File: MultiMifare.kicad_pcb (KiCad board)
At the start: 2 copper layers, 54 x 85.6 mm, 5 parts, among them SW1 SW_SPST, SW2 SW_SPST, U1 Mifare_Chip, U2 Mifare_Chip

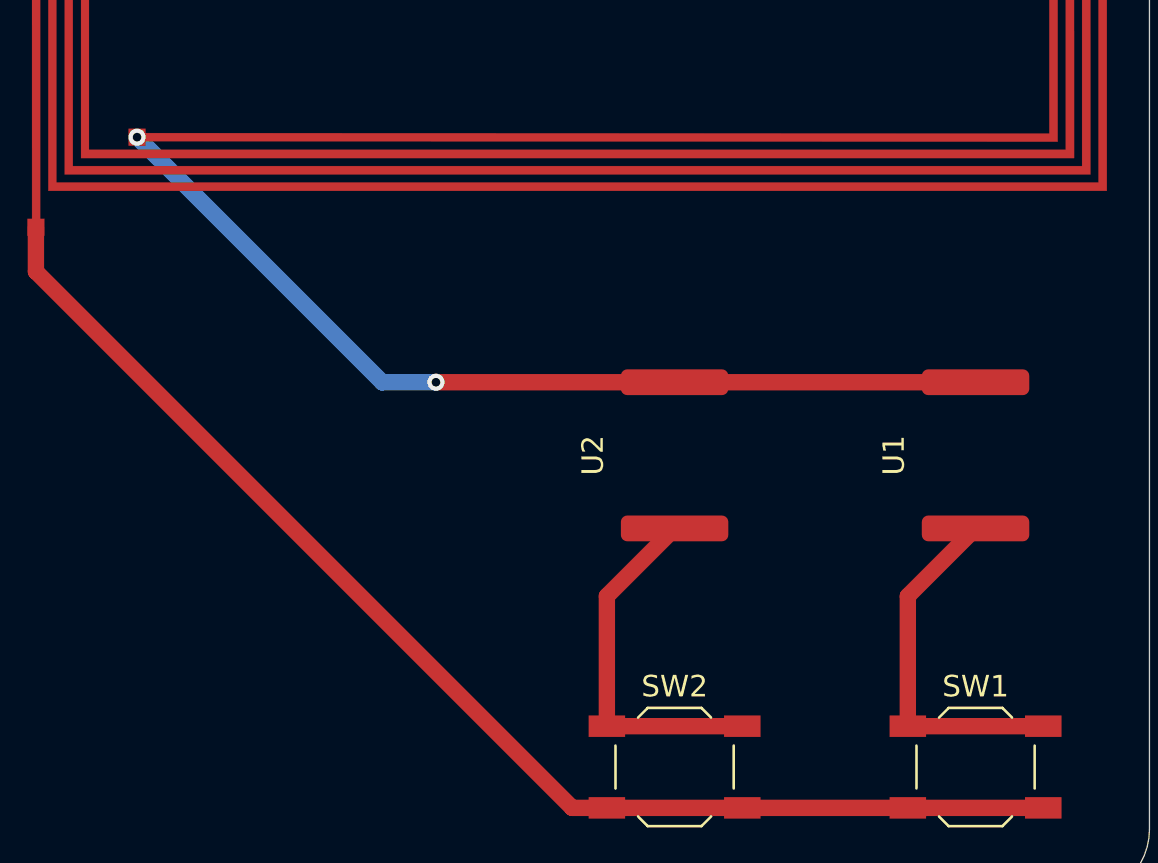
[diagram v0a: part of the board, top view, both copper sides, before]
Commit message: Easier to solder
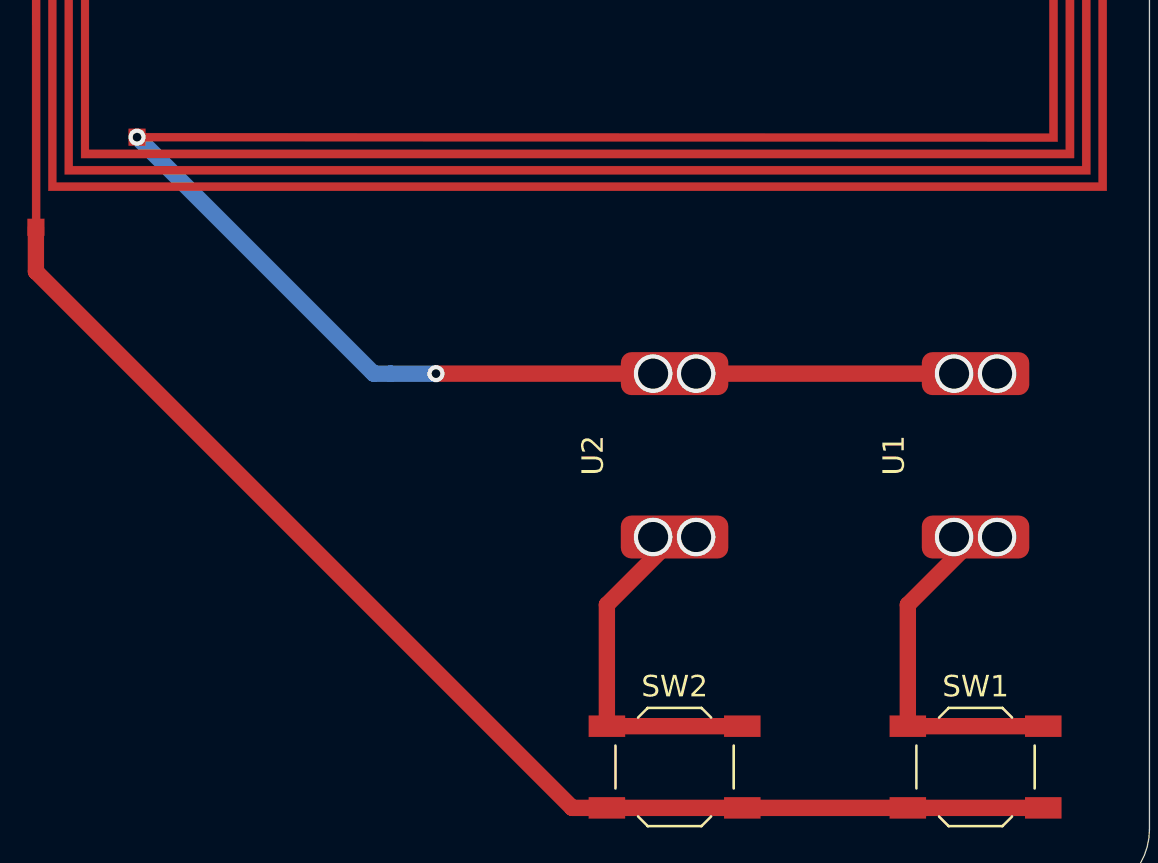
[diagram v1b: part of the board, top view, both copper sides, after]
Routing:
- net Net-(SW2-Pad1): track 16.8 -> 16.4 mm, vias 0 -> 2
- net Net-(SW1-Pad1): track 16.8 -> 16.4 mm, vias 0 -> 2
- net Net-(AE1-Pad2): track 43.7 -> 43.6 mm, vias 2 -> 6
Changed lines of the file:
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@@
     (thickness 1.6)
     (drawings 8)
-    (tracks 21)
+    (tracks 29)
     (zones 0)
     (modules 5)
@@
     (34 B.Paste user)
     (35 F.Paste user)
-    (36 B.SilkS user hide)
-    (37 F.SilkS user hide)
+    (36 B.SilkS user)
+    (37 F.SilkS user)
     (38 B.Mask user)
-    (39 F.Mask user hide)
+    (39 F.Mask user)
     (40 Dwgs.User user)
     (41 Cmts.User user)
@@
   )
   (setup
-    (last_trace_width 0.25)
+    (last_trace_width 0.762)
     (user_trace_width 0.254)
     (user_trace_width 0.508)
@@
       (effects (font (size 1 1) (thickness 0.15)))
     )
+    (fp_line (start -5.08 -2.8) (end 5.08 -2.8) (layer F.CrtYd) (width 0.12))
+    (fp_line (start 5.08 -2.8) (end 5.08 2.8) (layer F.CrtYd) (width 0.12))
+    (fp_line (start 5.08 2.8) (end -5.08 2.8) (layer F.CrtYd) (width 0.12))
+    (fp_line (start -5.08 2.8) (end -5.08 -2.8) (layer F.CrtYd) (width 0.12))
+    (fp_line (start -2.5 -2.4) (end 2.5 -2.4) (layer F.Fab) (width 0.12))
+    (fp_line (start 2.5 -2.4) (end 2.5 2.4) (layer F.Fab) (width 0.12))
+    (fp_line (start 2.5 2.4) (end -2.5 2.4) (layer F.Fab) (width 0.12))
     (fp_line (start -2.5 2.4) (end -2.5 -2.4) (layer F.Fab) (width 0.12))
-    (fp_line (start 2.5 2.4) (end -2.5 2.4) (layer F.Fab) (width 0.12))
-    (fp_line (start 2.5 -2.4) (end 2.5 2.4) (layer F.Fab) (width 0.12))
-    (fp_line (start -2.5 -2.4) (end 2.5 -2.4) (layer F.Fab) (width 0.12))
-    (fp_line (start -4.3 2.8) (end -4.3 -2.8) (layer F.CrtYd) (width 0.12))
-    (fp_line (start 4.3 2.8) (end -4.3 2.8) (layer F.CrtYd) (width 0.12))
-    (fp_line (start 4.3 -2.8) (end 4.3 2.8) (layer F.CrtYd) (width 0.12))
-    (fp_line (start -4.3 -2.8) (end 4.3 -2.8) (layer F.CrtYd) (width 0.12))
-    (pad 2 smd roundrect (at 3.4 0 270) (size 1.2 5) (layers F.Cu F.Paste F.Mask) (roundrect_rratio 0.25)
+    (pad 2 smd roundrect (at 3.8 0 270) (size 2 5) (layers F.Cu F.Paste F.Mask) (roundrect_rratio 0.25)
       (net 2 "Net-(SW2-Pad1)"))
-    (pad 1 smd roundrect (at -3.4 0 270) (size 1.2 5) (layers F.Cu F.Paste F.Mask) (roundrect_rratio 0.25)
+    (pad 1 smd roundrect (at -3.8 0 270) (size 2 5) (layers F.Cu F.Paste F.Mask) (roundrect_rratio 0.25)
       (net 4 "Net-(AE1-Pad2)"))
   )
@@
       (effects (font (size 1 1) (thickness 0.15)))
     )
+    (fp_line (start -5.08 -2.8) (end 5.08 -2.8) (layer F.CrtYd) (width 0.12))
+    (fp_line (start 5.08 -2.8) (end 5.08 2.8) (layer F.CrtYd) (width 0.12))
+    (fp_line (start 5.08 2.8) (end -5.08 2.8) (layer F.CrtYd) (width 0.12))
+    (fp_line (start -5.08 2.8) (end -5.08 -2.8) (layer F.CrtYd) (width 0.12))
+    (fp_line (start -2.5 -2.4) (end 2.5 -2.4) (layer F.Fab) (width 0.12))
+    (fp_line (start 2.5 -2.4) (end 2.5 2.4) (layer F.Fab) (width 0.12))
+    (fp_line (start 2.5 2.4) (end -2.5 2.4) (layer F.Fab) (width 0.12))
     (fp_line (start -2.5 2.4) (end -2.5 -2.4) (layer F.Fab) (width 0.12))
-    (fp_line (start 2.5 2.4) (end -2.5 2.4) (layer F.Fab) (width 0.12))
-    (fp_line (start 2.5 -2.4) (end 2.5 2.4) (layer F.Fab) (width 0.12))
-    (fp_line (start -2.5 -2.4) (end 2.5 -2.4) (layer F.Fab) (width 0.12))
-    (fp_line (start -4.3 2.8) (end -4.3 -2.8) (layer F.CrtYd) (width 0.12))
-    (fp_line (start 4.3 2.8) (end -4.3 2.8) (layer F.CrtYd) (width 0.12))
-    (fp_line (start 4.3 -2.8) (end 4.3 2.8) (layer F.CrtYd) (width 0.12))
-    (fp_line (start -4.3 -2.8) (end 4.3 -2.8) (layer F.CrtYd) (width 0.12))
-    (pad 2 smd roundrect (at 3.4 0 270) (size 1.2 5) (layers F.Cu F.Paste F.Mask) (roundrect_rratio 0.25)
+    (pad 2 smd roundrect (at 3.8 0 270) (size 2 5) (layers F.Cu F.Paste F.Mask) (roundrect_rratio 0.25)
       (net 1 "Net-(SW1-Pad1)"))
-    (pad 1 smd roundrect (at -3.4 0 270) (size 1.2 5) (layers F.Cu F.Paste F.Mask) (roundrect_rratio 0.25)
+    (pad 1 smd roundrect (at -3.8 0 270) (size 2 5) (layers F.Cu F.Paste F.Mask) (roundrect_rratio 0.25)
       (net 4 "Net-(AE1-Pad2)"))
   )
@@
     )
     (fp_text value SW_SPST (at 0 3.75) (layer F.Fab)
+      (effects (font (size 1 1) (thickness 0.15)))
+    )
+    (fp_text user %R (at 0 -3.75) (layer F.Fab)
       (effects (font (size 1 1) (thickness 0.15)))
     )
@@
     (fp_line (start -4.25 3) (end -4.25 -3) (layer F.CrtYd) (width 0.05))
     (fp_circle (center 0 0) (end 1 0) (layer F.Fab) (width 0.1))
-    (fp_text user %R (at 0 -3.75) (layer F.Fab)
-      (effects (font (size 1 1) (thickness 0.15)))
-    )
     (pad 2 smd rect (at 3.15 1.9) (size 1.7 1) (layers F.Cu F.Paste F.Mask)
       (net 3 "Net-(AE1-Pad1)"))
@@
     )
     (fp_text value SW_SPST (at 0 3.75) (layer F.Fab)
+      (effects (font (size 1 1) (thickness 0.15)))
+    )
+    (fp_text user %R (at 0 -3.75) (layer F.Fab)
       (effects (font (size 1 1) (thickness 0.15)))
     )
@@
     (fp_line (start -4.25 3) (end -4.25 -3) (layer F.CrtYd) (width 0.05))
     (fp_circle (center 0 0) (end 1 0) (layer F.Fab) (width 0.1))
-    (fp_text user %R (at 0 -3.75) (layer F.Fab)
-      (effects (font (size 1 1) (thickness 0.15)))
-    )
     (pad 2 smd rect (at 3.15 1.9) (size 1.7 1) (layers F.Cu F.Paste F.Mask)
       (net 3 "Net-(AE1-Pad1)"))
@@
   (gr_line (start 179.09 58.16) (end 179.09 137.4) (layer Edge.Cuts) (width 0.05))
   (gr_line (start 128.29 54.98) (end 175.91 54.98) (layer Edge.Cuts) (width 0.05))
-  (segment (start 167.85 126.55) (end 171 123.4) (width 0.762) (layer F.Cu) (net 1))
-  (segment (start 167.85 132.6) (end 167.85 126.55) (width 0.762) (layer F.Cu) (net 1))
+  (via (at 172 123.8) (size 1.8) (drill 1.4) (layers F.Cu B.Cu) (net 1))
+  (via (at 170 123.8) (size 1.8) (drill 1.4) (layers F.Cu B.Cu) (net 1))
+  (via (at 156 123.8) (size 1.8) (drill 1.4) (layers F.Cu B.Cu) (net 2))
+  (via (at 158 123.8) (size 1.8) (drill 1.4) (layers F.Cu B.Cu) (net 2))
+  (via (at 172 116.2) (size 1.8) (drill 1.4) (layers F.Cu B.Cu) (net 4))
+  (via (at 170 116.2) (size 1.8) (drill 1.4) (layers F.Cu B.Cu) (net 4))
+  (via (at 158 116.2) (size 1.8) (drill 1.4) (layers F.Cu B.Cu) (net 4))
   (segment (start 174.15 132.6) (end 167.85 132.6) (width 0.762) (layer F.Cu) (net 1))
+  (segment (start 167.85 126.95) (end 171 123.8) (width 0.762) (layer F.Cu) (net 1))
+  (segment (start 167.85 132.6) (end 167.85 126.95) (width 0.762) (layer F.Cu) (net 1))
   (segment (start 160.15 132.6) (end 153.85 132.6) (width 0.762) (layer F.Cu) (net 2))
-  (segment (start 153.85 126.55) (end 157 123.4) (width 0.762) (layer F.Cu) (net 2))
-  (segment (start 153.85 132.6) (end 153.85 126.55) (width 0.762) (layer F.Cu) (net 2))
+  (segment (start 153.85 126.95) (end 157 123.8) (width 0.762) (layer F.Cu) (net 2))
+  (segment (start 153.85 132.6) (end 153.85 126.95) (width 0.762) (layer F.Cu) (net 2))
   (segment (start 174.15 136.4) (end 167.85 136.4) (width 0.762) (layer F.Cu) (net 3))
   (segment (start 167.85 136.4) (end 160.15 136.4) (width 0.762) (layer F.Cu) (net 3))
@@
   (segment (start 152.238 136.4) (end 127.29 111.452) (width 0.762) (layer F.Cu) (net 3))
   (segment (start 127.29 111.452) (end 127.29 109.392) (width 0.762) (layer F.Cu) (net 3))
-  (segment (start 171 116.6) (end 157 116.6) (width 0.762) (layer F.Cu) (net 4))
-  (via (at 145.9 116.6) (size 0.8) (drill 0.4) (layers F.Cu B.Cu) (net 4))
-  (segment (start 157 116.6) (end 145.9 116.6) (width 0.762) (layer F.Cu) (net 4))
-  (segment (start 143.394 116.6) (end 143.394 116.594) (width 0.762) (layer B.Cu) (net 4))
   (via (at 131.994 105.2) (size 0.8) (drill 0.4) (layers F.Cu B.Cu) (net 4))
+  (via (at 145.9 116.2) (size 0.8) (drill 0.4) (layers F.Cu B.Cu) (net 4))
+  (segment (start 143.788 116.2) (end 145.9 116.2) (width 0.762) (layer B.Cu) (net 4))
   (segment (start 132 105.2) (end 131.994 105.2) (width 0.762) (layer B.Cu) (net 4))
-  (segment (start 143.394 116.594) (end 132 105.2) (width 0.762) (layer B.Cu) (net 4))
-  (segment (start 143.4 116.6) (end 143.394 116.594) (width 0.762) (layer B.Cu) (net 4))
-  (segment (start 145.9 116.6) (end 143.4 116.6) (width 0.762) (layer B.Cu) (net 4))
+  (segment (start 143 116.2) (end 132 105.2) (width 0.762) (layer B.Cu) (net 4))
+  (segment (start 143.8 116.2) (end 143 116.2) (width 0.762) (layer B.Cu) (net 4))
+  (segment (start 171 116.2) (end 157 116.2) (width 0.762) (layer F.Cu) (net 4))
+  (segment (start 157 116.2) (end 156 116.2) (width 0.762) (layer F.Cu) (net 4))
+  (segment (start 156 116.2) (end 145.9 116.2) (width 0.762) (layer F.Cu) (net 4))
+  (via (at 156 116.2) (size 1.8) (drill 1.4) (layers F.Cu B.Cu) (net 4))
 )
